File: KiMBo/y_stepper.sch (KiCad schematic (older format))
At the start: 25 parts, among them U24 TMC2130

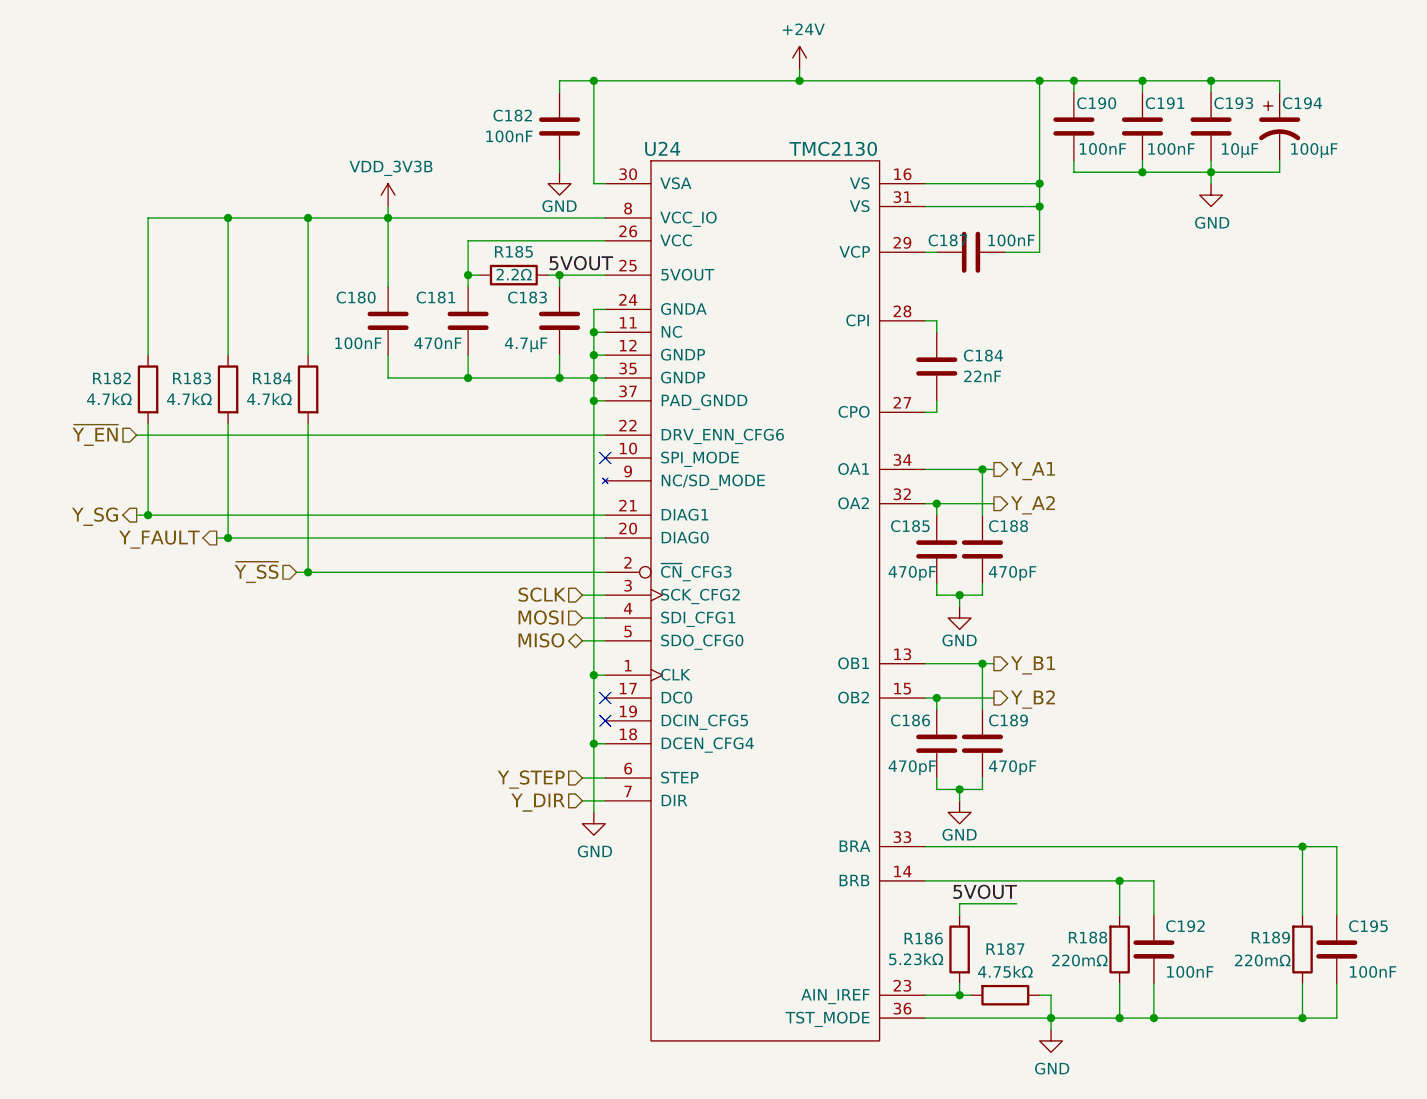
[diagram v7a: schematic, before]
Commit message: Remove HDMI from the schematic
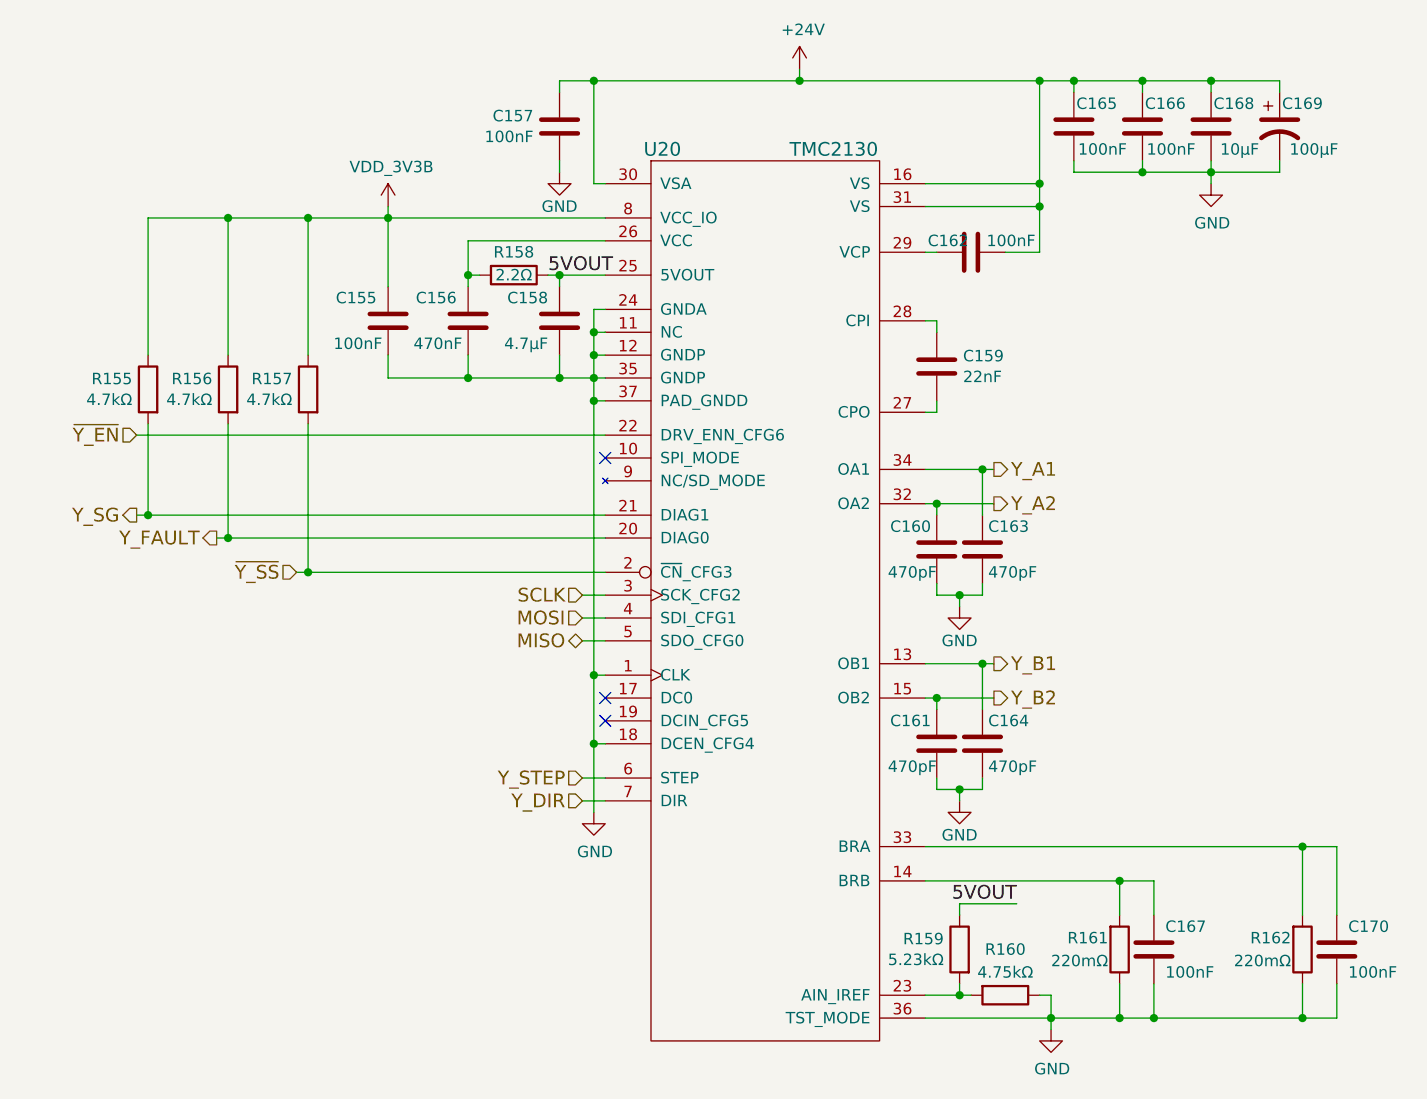
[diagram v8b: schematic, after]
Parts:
- renumbered C180 to C155, C181 to C156, C182 to C157, C183 to C158, C184 to C159, C185 to C160, C186 to C161, C187 to C162, C188 to C163, C189 to C164, C190 to C165, C191 to C166, C192 to C167, C193 to C168, C194 to C169, C195 to C170, R182 to R155, R183 to R156, R184 to R157, R185 to R158, R186 to R159, R187 to R160, R188 to R161, R189 to R162, U24 to U20
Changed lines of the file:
@@
 $Descr A3 16535 11693
 encoding utf-8
-Sheet 22 26
+Sheet 22 25
 Title ""
 Date ""
@@
 Y_SG
 $Comp
-L C C182
+L C C157
 U 1 1 58C0B215
 P 6550 3250
-F 0 "C182" H 6436 3204 50  0000 R CNN
+F 0 "C157" H 6436 3204 50  0000 R CNN
 F 1 "100nF" H 6436 3295 50  0000 R CNN
 F 2 "Capacitors_SMD:C_0603" H 6588 3100 50  0001 C CNN
@@
 $EndComp
 $Comp
-L C C187
+L C C162
 U 1 1 58C0B21C
 P 8350 3800
-F 0 "C187" V 8300 3700 50  0000 C CNN
+F 0 "C162" V 8300 3700 50  0000 C CNN
 F 1 "100nF" V 8300 3975 50  0000 C CNN
 F 2 "Capacitors_SMD:C_0603" H 8388 3650 50  0001 C CNN
@@
 $EndComp
 $Comp
-L CP1 C194
+L CP1 C169
 U 1 1 58C0B223
 P 9700 3250
-F 0 "C194" H 9800 3350 50  0000 C CNN
+F 0 "C169" H 9800 3350 50  0000 C CNN
 F 1 "100μF" H 9850 3150 50  0000 C CNN
 F 2 "Capacitors_SMD:c_elec_8x10" H 9700 3250 50  0001 C CNN
@@
 $EndComp
 $Comp
-L C C190
+L C C165
 U 1 1 58C0B22A
 P 8800 3250
-F 0 "C190" H 8700 3350 50  0000 C CNN
+F 0 "C165" H 8700 3350 50  0000 C CNN
 F 1 "100nF" H 8675 3150 50  0000 C CNN
 F 2 "Capacitors_SMD:C_0603" H 8838 3100 50  0001 C CNN
@@
 $EndComp
 $Comp
-L GND #PWR0248
+L GND #PWR0217
 U 1 1 58C0B231
 P 6550 3450
-F 0 "#PWR0248" H 6550 3200 50  0001 C CNN
+F 0 "#PWR0217" H 6550 3200 50  0001 C CNN
 F 1 "GND" H 6550 3300 50  0000 C CNN
 F 2 "" H 6550 3450 50  0000 C CNN
@@
 $EndComp
 $Comp
-L C C191
+L C C166
 U 1 1 58C0B237
 P 9100 3250
-F 0 "C191" H 9000 3350 50  0000 C CNN
+F 0 "C166" H 9000 3350 50  0000 C CNN
 F 1 "100nF" H 8975 3150 50  0000 C CNN
 F 2 "Capacitors_SMD:C_0603" H 9138 3100 50  0001 C CNN
@@
 $EndComp
 $Comp
-L GND #PWR0249
+L GND #PWR0218
 U 1 1 58C0B23E
 P 9400 3500
-F 0 "#PWR0249" H 9400 3250 50  0001 C CNN
+F 0 "#PWR0218" H 9400 3250 50  0001 C CNN
 F 1 "GND" H 9405 3327 50  0000 C CNN
 F 2 "" H 9400 3500 50  0000 C CNN
@@
 $EndComp
 $Comp
-L +24V #PWR0250
+L +24V #PWR0219
 U 1 1 58C0B244
 P 7600 3000
-F 0 "#PWR0250" H 7600 2850 50  0001 C CNN
+F 0 "#PWR0219" H 7600 2850 50  0001 C CNN
 F 1 "+24V" H 7615 3173 50  0000 C CNN
 F 2 "" H 7600 3000 50  0000 C CNN
@@
 $EndComp
 $Comp
-L C C184
+L C C159
 U 1 1 58C0B24A
 P 8200 4300
-F 0 "C184" H 8315 4346 50  0000 L CNN
+F 0 "C159" H 8315 4346 50  0000 L CNN
 F 1 "22nF" H 8315 4255 50  0000 L CNN
 F 2 "Capacitors_SMD:C_0603" H 8238 4150 50  0001 C CNN
@@
 $EndComp
 $Comp
-L R R189
+L R R162
 U 1 1 58C0B251
 P 9800 6850
-F 0 "R189" H 9750 6800 50  0000 R CNN
+F 0 "R162" H 9750 6800 50  0000 R CNN
 F 1 "220mΩ" H 9750 6900 50  0000 R CNN
 F 2 "Resistors_SMD:R_0805" V 9730 6850 50  0001 C CNN
@@
 $EndComp
 $Comp
-L R R188
+L R R161
 U 1 1 58C0B258
 P 9000 6850
-F 0 "R188" H 8950 6800 50  0000 R CNN
+F 0 "R161" H 8950 6800 50  0000 R CNN
 F 1 "220mΩ" H 8950 6900 50  0000 R CNN
 F 2 "Resistors_SMD:R_0805" V 8930 6850 50  0001 C CNN
@@
 $EndComp
 $Comp
-L GND #PWR0251
+L GND #PWR0220
 U 1 1 58C0B25F
 P 8700 7200
-F 0 "#PWR0251" H 8700 6950 50  0001 C CNN
+F 0 "#PWR0220" H 8700 6950 50  0001 C CNN
 F 1 "GND" H 8705 7027 50  0000 C CNN
 F 2 "" H 8700 7200 50  0000 C CNN
@@
 NoConn ~ 6750 5750
 $Comp
-L R R185
+L R R158
 U 1 1 58C0B266
 P 6350 3900
-F 0 "R185" V 6250 3900 50  0000 C CNN
+F 0 "R158" V 6250 3900 50  0000 C CNN
 F 1 "2.2Ω" V 6350 3900 50  0000 C CNN
 F 2 "Resistors_SMD:R_0603" V 6280 3900 50  0001 C CNN
@@
 $EndComp
 $Comp
-L C C181
+L C C156
 U 1 1 58C0B26D
 P 6150 4100
-F 0 "C181" H 6200 4200 50  0000 L CNN
+F 0 "C156" H 6200 4200 50  0000 L CNN
 F 1 "470nF" H 6175 4000 50  0000 L CNN
 F 2 "Capacitors_SMD:C_0603" H 6188 3950 50  0001 C CNN
@@
 NoConn ~ 6750 5850
 $Comp
-L GND #PWR0252
+L GND #PWR0221
 U 1 1 58C0B282
 P 6700 6250
-F 0 "#PWR0252" H 6700 6000 50  0001 C CNN
+F 0 "#PWR0221" H 6700 6000 50  0001 C CNN
 F 1 "GND" H 6705 6077 50  0000 C CNN
 F 2 "" H 6700 6250 50  0000 C CNN
@@
 $EndComp
 $Comp
-L C C192
+L C C167
 U 1 1 58C0B288
 P 9150 6850
-F 0 "C192" H 9200 6950 50  0000 L CNN
+F 0 "C167" H 9200 6950 50  0000 L CNN
 F 1 "100nF" H 9200 6750 50  0000 L CNN
 F 2 "Capacitors_SMD:C_0603" H 9188 6700 50  0001 C CNN
@@
 Y_FAULT
 $Comp
-L R R183
+L R R156
 U 1 1 58C0B290
 P 5100 4400
-F 0 "R183" H 5169 4446 50  0000 L CNN
+F 0 "R156" H 5169 4446 50  0000 L CNN
 F 1 "4.7kΩ" H 5169 4355 50  0000 L CNN
 F 2 "Resistors_SMD:R_0603" V 5030 4400 50  0001 C CNN
@@
 NoConn ~ 6750 4700
 $Comp
-L C C183
+L C C158
 U 1 1 58C0B29A
 P 6550 4100
-F 0 "C183" H 6600 4200 50  0000 L CNN
+F 0 "C158" H 6600 4200 50  0000 L CNN
 F 1 "4.7μF" H 6600 4000 50  0000 L CNN
 F 2 "Capacitors_SMD:C_0603" H 6588 3950 50  0001 C CNN
@@
 5VOUT
 $Comp
-L R R186
+L R R159
 U 1 1 58C0B2A2
 P 8300 6850
-F 0 "R186" H 8369 6896 50  0000 L CNN
+F 0 "R159" H 8369 6896 50  0000 L CNN
 F 1 "5.23kΩ" H 8369 6805 50  0000 L CNN
 F 2 "Resistors_SMD:R_0603" V 8230 6850 50  0001 C CNN
@@
 5VOUT
 $Comp
-L R R187
+L R R160
 U 1 1 58C0B2AA
 P 8500 7050
-F 0 "R187" V 8300 7050 50  0000 C CNN
+F 0 "R160" V 8300 7050 50  0000 C CNN
 F 1 "4.75kΩ" V 8400 7050 50  0000 C CNN
 F 2 "Resistors_SMD:R_0603" V 8430 7050 50  0001 C CNN
@@
 $EndComp
 $Comp
-L R R184
+L R R157
 U 1 1 58C0B2B1
 P 5450 4400
-F 0 "R184" H 5519 4446 50  0000 L CNN
+F 0 "R157" H 5519 4446 50  0000 L CNN
 F 1 "4.7kΩ" H 5519 4355 50  0000 L CNN
 F 2 "Resistors_SMD:R_0603" V 5380 4400 50  0001 C CNN
@@
 $EndComp
 $Comp
-L C C195
+L C C170
 U 1 1 58C0B2B8
 P 9950 6850
-F 0 "C195" H 10000 6950 50  0000 L CNN
+F 0 "C170" H 10000 6950 50  0000 L CNN
 F 1 "100nF" H 10000 6750 50  0000 L CNN
 F 2 "Capacitors_SMD:C_0603" H 9988 6700 50  0001 C CNN
@@
 $EndComp
 $Comp
-L C C185
+L C C160
 U 1 1 58C0B2BF
 P 8200 5100
-F 0 "C185" H 8225 5200 50  0000 L CNN
+F 0 "C160" H 8225 5200 50  0000 L CNN
 F 1 "470pF" H 8200 5000 50  0000 L CNN
 F 2 "Capacitors_SMD:C_0603" H 8238 4950 50  0001 C CNN
@@
 $EndComp
 $Comp
-L GND #PWR0253
+L GND #PWR0222
 U 1 1 58C0B2C6
 P 8300 5350
-F 0 "#PWR0253" H 8300 5100 50  0001 C CNN
+F 0 "#PWR0222" H 8300 5100 50  0001 C CNN
 F 1 "GND" H 8300 5200 50  0000 C CNN
 F 2 "" H 8300 5350 50  0000 C CNN
@@
 $EndComp
 $Comp
-L C C188
+L C C163
 U 1 1 58C0B2CC
 P 8400 5100
-F 0 "C188" H 8425 5200 50  0000 L CNN
+F 0 "C163" H 8425 5200 50  0000 L CNN
 F 1 "470pF" H 8425 5000 50  0000 L CNN
 F 2 "Capacitors_SMD:C_0603" H 8438 4950 50  0001 C CNN
@@
 $EndComp
 $Comp
-L C C186
+L C C161
 U 1 1 58C0B2D3
 P 8200 5950
-F 0 "C186" H 8225 6050 50  0000 L CNN
+F 0 "C161" H 8225 6050 50  0000 L CNN
 F 1 "470pF" H 8200 5850 50  0000 L CNN
 F 2 "Capacitors_SMD:C_0603" H 8238 5800 50  0001 C CNN
@@
 $EndComp
 $Comp
-L GND #PWR0254
+L GND #PWR0223
 U 1 1 58C0B2DA
 P 8300 6200
-F 0 "#PWR0254" H 8300 5950 50  0001 C CNN
+F 0 "#PWR0223" H 8300 5950 50  0001 C CNN
 F 1 "GND" H 8300 6050 50  0000 C CNN
 F 2 "" H 8300 6200 50  0000 C CNN
@@
 $EndComp
 $Comp
-L C C189
+L C C164
 U 1 1 58C0B2E0
 P 8400 5950
-F 0 "C189" H 8425 6050 50  0000 L CNN
+F 0 "C164" H 8425 6050 50  0000 L CNN
 F 1 "470pF" H 8425 5850 50  0000 L CNN
 F 2 "Capacitors_SMD:C_0603" H 8438 5800 50  0001 C CNN
@@
 $EndComp
 $Comp
-L TMC2130 U24
+L TMC2130 U20
 U 1 1 58C0B2E7
 P 7450 4850
-F 0 "U24" H 7000 6350 60  0000 C CNN
+F 0 "U20" H 7000 6350 60  0000 C CNN
 F 1 "TMC2130" H 7750 6350 60  0000 C CNN
 F 2 "KiMBo:QFN36_5X6" H 7450 5150 60  0001 C CNN
@@
 	8200 6150 8200 6100
 $Comp
-L R R182
+L R R155
 U 1 1 58C0B35B
 P 4750 4400
-F 0 "R182" H 4819 4446 50  0000 L CNN
+F 0 "R155" H 4819 4446 50  0000 L CNN
 F 1 "4.7kΩ" H 4819 4355 50  0000 L CNN
 F 2 "Resistors_SMD:R_0603" V 4680 4400 50  0001 C CNN
@@
 Connection ~ 5100 3650
 $Comp
-L C C193
+L C C168
 U 1 1 58C0B366
 P 9400 3250
-F 0 "C193" H 9300 3350 50  0000 C CNN
+F 0 "C168" H 9300 3350 50  0000 C CNN
 F 1 "10μF" H 9275 3150 50  0000 C CNN
 F 2 "Capacitors_SMD:C_0805" H 9438 3100 50  0001 C CNN
@@
 	4750 3650 6750 3650
 $Comp
-L VDD_3V3B #PWR0255
+L VDD_3V3B #PWR0224
 U 1 1 5A300CA5
 P 5800 3600
-F 0 "#PWR0255" H 5800 3450 50  0001 C CNN
+F 0 "#PWR0224" H 5800 3450 50  0001 C CNN
 F 1 "VDD_3V3B" H 5815 3773 50  0000 C CNN
 F 2 "" H 5800 3600 50  0000 C CNN
@@
 $EndComp
 $Comp
-L C C180
+L C C155
 U 1 1 5A89AE9E
 P 5800 4100
-F 0 "C180" H 5850 4200 50  0000 L CNN
+F 0 "C155" H 5850 4200 50  0000 L CNN
 F 1 "100nF" H 5825 4000 50  0000 L CNN
 F 2 "Capacitors_SMD:C_0603" H 5838 3950 50  0001 C CNN
